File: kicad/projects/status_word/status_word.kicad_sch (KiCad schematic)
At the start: 54 parts, among them J1 peripheral_addr_bus_connector, J10 Conn_01x02_Pin, J11 Conn_01x02_Pin, J12 Conn_01x02_Pin, J13 Conn_01x02_Pin, J14 Conn_01x08_Socket, J15 Conn_01x03_Pin, J2 peripheral_aux_connector, J3 peripheral_membank_connector, J4 Conn_01x16_Socket, J5 Conn_01x04_Socket, J6 Conn_01x02_Pin, J7 Conn_01x02_Pin, J8 Conn_01x02_Pin, J9 Conn_01x02_Pin, U1 74HC10, U2 74HC377, U3 74HC377, U4 74HC245, U5 74HC245, U6 74HC245, U7 74HC245

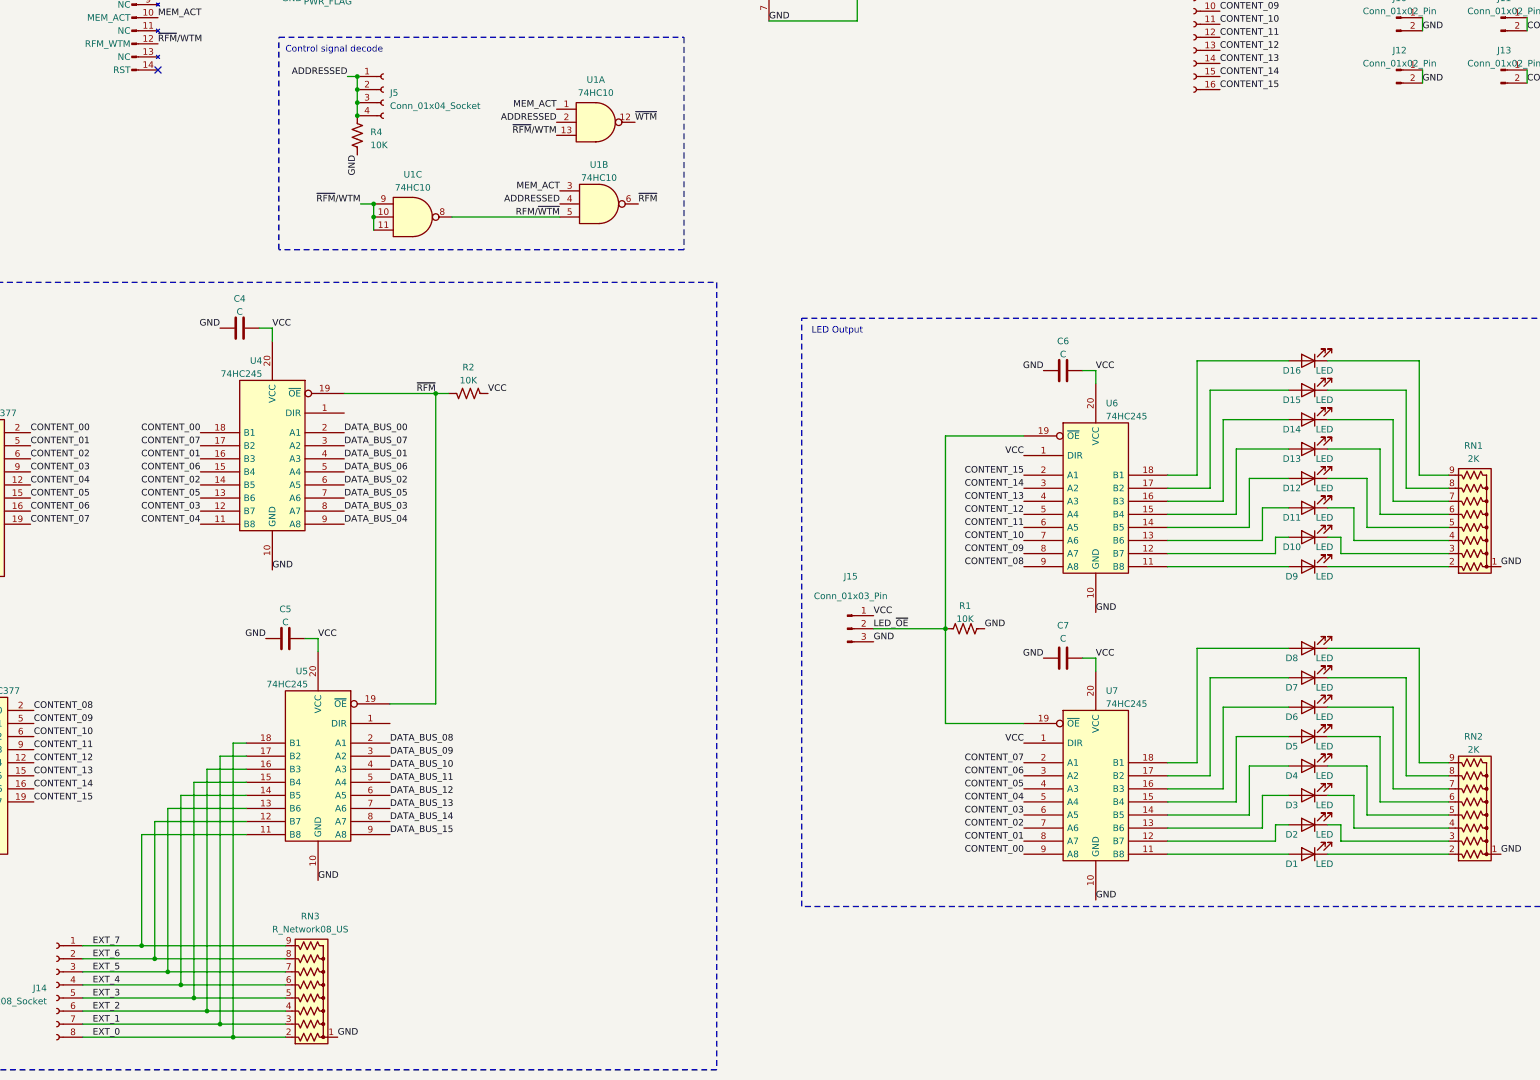
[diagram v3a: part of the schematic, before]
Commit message: Status word PCB done - just needs tech check.
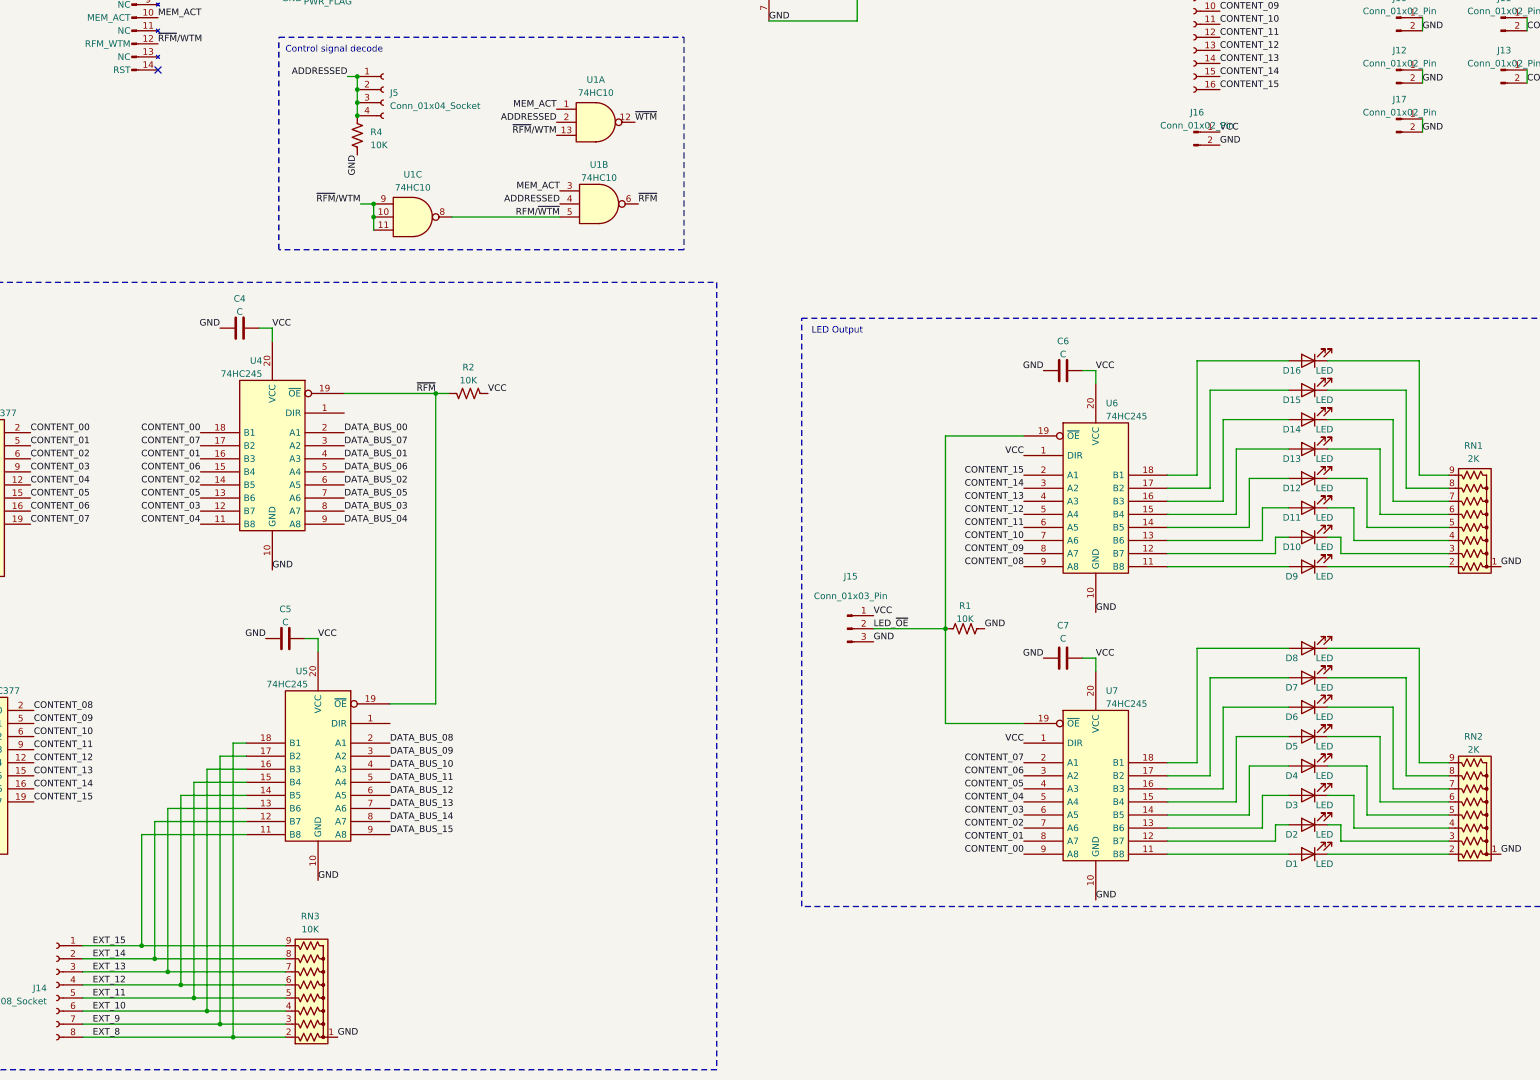
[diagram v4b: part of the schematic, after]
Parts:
- added J16: Conn_01x02_Pin, Connector_PinSocket_2.54mm:PinSocket_1x02_P2.54mm_Horizontal, symbol Connector:Conn_01x02_Pin
- added J17: Conn_01x02_Pin, Connector_PinHeader_2.54mm:PinHeader_1x02_P2.54mm_Vertical, symbol Connector:Conn_01x02_Pin
- RN3: value R_Network08_US -> 10K
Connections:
- net GND: now also J16.2 (Pin_2), J17.1 (Pin_1), J17.2 (Pin_2)
- net VCC: now also J16.1 (Pin_1)
- net EXT_0 renamed EXT_8
- net EXT_1 renamed EXT_9
- net EXT_2 renamed EXT_10
- net EXT_3 renamed EXT_11
- net EXT_4 renamed EXT_12
- net EXT_5 renamed EXT_13
- net EXT_6 renamed EXT_14
- net EXT_7 renamed EXT_15
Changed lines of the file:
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@@
+    (stroke (width 0) (type default))
+  )
+  (wire (pts (xy 360.045 67.945) (xy 360.045 70.485))
     (stroke (width 0) (type default))
   )
@@
     (effects (font (size 1.27 1.27)) (justify left bottom))
   )
-  (label "EXT_0" (at 101.6 246.38 0) (fields_autoplaced)
+  (label "EXT_8" (at 101.6 246.38 0) (fields_autoplaced)
     (effects (font (size 1.27 1.27)) (justify left bottom))
   )
@@
     (effects (font (size 1.27 1.27)) (justify left bottom))
   )
+  (label "VCC" (at 320.675 70.485 0) (fields_autoplaced)
+    (effects (font (size 1.27 1.27)) (justify left bottom))
+  )
   (label "CONTENT_09" (at 282.575 152.4 180) (fields_autoplaced)
     (effects (font (size 1.27 1.27)) (justify right bottom))
@@
     (effects (font (size 1.27 1.27)) (justify left bottom))
   )
-  (label "EXT_4" (at 101.6 236.22 0) (fields_autoplaced)
+  (label "EXT_12" (at 101.6 236.22 0) (fields_autoplaced)
     (effects (font (size 1.27 1.27)) (justify left bottom))
   )
@@
     (effects (font (size 1.27 1.27)) (justify left bottom))
   )
-  (label "EXT_7" (at 101.6 228.6 0) (fields_autoplaced)
+  (label "EXT_15" (at 101.6 228.6 0) (fields_autoplaced)
     (effects (font (size 1.27 1.27)) (justify left bottom))
   )
@@
     (effects (font (size 1.27 1.27)) (justify left bottom))
   )
-  (label "EXT_2" (at 101.6 241.3 0) (fields_autoplaced)
+  (label "EXT_10" (at 101.6 241.3 0) (fields_autoplaced)
     (effects (font (size 1.27 1.27)) (justify left bottom))
   )
@@
     (effects (font (size 1.27 1.27)) (justify right bottom))
   )
+  (label "GND" (at 360.045 70.485 0) (fields_autoplaced)
+    (effects (font (size 1.27 1.27)) (justify left bottom))
+  )
   (label "CONTENT_08" (at 320.675 44.45 0) (fields_autoplaced)
     (effects (font (size 1.27 1.27)) (justify left bottom))
   )
+  (label "GND" (at 320.675 73.025 0) (fields_autoplaced)
+    (effects (font (size 1.27 1.27)) (justify left bottom))
+  )
   (label "DATA_BUS_06" (at 64.135 144.145 180) (fields_autoplaced)
     (effects (font (size 1.27 1.27)) (justify right bottom))
@@
     (effects (font (size 1.27 1.27)) (justify right bottom))
   )
-  (label "EXT_1" (at 101.6 243.84 0) (fields_autoplaced)
+  (label "EXT_9" (at 101.6 243.84 0) (fields_autoplaced)
     (effects (font (size 1.27 1.27)) (justify left bottom))
   )
@@
     (effects (font (size 1.27 1.27)) (justify left bottom))
   )
-  (label "EXT_6" (at 101.6 231.14 0) (fields_autoplaced)
+  (label "EXT_14" (at 101.6 231.14 0) (fields_autoplaced)
     (effects (font (size 1.27 1.27)) (justify left bottom))
   )
@@
     (effects (font (size 1.27 1.27)) (justify right bottom))
   )
-  (label "EXT_5" (at 101.6 233.68 0) (fields_autoplaced)
+  (label "EXT_13" (at 101.6 233.68 0) (fields_autoplaced)
     (effects (font (size 1.27 1.27)) (justify left bottom))
   )
@@
     (effects (font (size 1.27 1.27)) (justify right bottom))
   )
-  (label "EXT_3" (at 101.6 238.76 0) (fields_autoplaced)
+  (label "EXT_11" (at 101.6 238.76 0) (fields_autoplaced)
     (effects (font (size 1.27 1.27)) (justify left bottom))
   )
@@
         (path "/0c25b387-1696-4e3f-ab8e-df646088b074"
           (reference "J15") (unit 1)
+        )
+      )
+    )
+  )
+  (symbol (lib_id "Connector:Conn_01x02_Pin") (at 354.965 67.945 0) (unit 1)
+    (in_bom yes) (on_board yes) (dnp no) (fields_autoplaced)
+    (property "Reference" "J17" (at 355.6 64.135 0)
+      (effects (font (size 1.27 1.27)))
+    )
+    (property "Value" "Conn_01x02_Pin" (at 355.6 66.675 0)
+      (effects (font (size 1.27 1.27)))
+    )
+    (property "Footprint" "Connector_PinHeader_2.54mm:PinHeader_1x02_P2.54mm_Vertical" (at 354.965 67.945 0)
+      (effects (font (size 1.27 1.27)) hide)
+    )
+    (property "Datasheet" "~" (at 354.965 67.945 0)
+      (effects (font (size 1.27 1.27)) hide)
+    )
+    (pin "1")
+    (pin "2")
+    (instances
+      (project "status_word"
+        (path "/0c25b387-1696-4e3f-ab8e-df646088b074"
+          (reference "J17") (unit 1)
         )
       )
@@
       (effects (font (size 1.27 1.27)))
     )
-    (property "Value" "R_Network08_US" (at 143.891 225.425 90)
+    (property "Value" "10K" (at 143.891 225.425 90)
       (effects (font (size 1.27 1.27)))
     )
@@
         )
       )
+    )
+  )
+  (symbol (lib_id "Connector:Conn_01x02_Pin") (at 315.595 70.485 0) (unit 1)
+    (in_bom yes) (on_board yes) (dnp no) (fields_autoplaced)
+    (property "Reference" "J16" (at 316.23 66.675 0)
+      (effects (font (size 1.27 1.27)))
+    )
+    (property "Value" "Conn_01x02_Pin" (at 316.23 69.215 0)
+      (effects (font (size 1.27 1.27)))
+    )
+    (property "Footprint" "Connector_PinSocket_2.54mm:PinSocket_1x02_P2.54mm_Horizontal" (at 315.595 70.485 0)
+      (effects (font (size 1.27 1.27)) hide)
+    )
+    (property "Datasheet" "~" (at 315.595 70.485 0)
+      (effects (font (size 1.27 1.27)) hide)
+    )
+    (pin "1")
+    (pin "2")
+    (instances
+      (project "status_word"
+        (path "/0c25b387-1696-4e3f-ab8e-df646088b074"
+          (reference "J16") (unit 1)
+        )
+      )

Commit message: Tech check on status word complete
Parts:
- C97, C98, C99: value C_Polarized -> 33uF
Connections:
- net GND: now also U4.1 (DIR), U5.1 (DIR)
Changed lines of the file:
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@@
 (kicad_sch (version 20230121) (generator eeschema)
   (paper "B")
+  (bus_alias "DATA_BUS" (members "DATA_BUS_00" "DATA_BUS_01" "DATA_BUS_02" "DATA_BUS_03" "DATA_BUS_04" "DATA_BUS_05" "DATA_BUS_06" "DATA_BUS_07" "DATA_BUS_08" "DATA_BUS_09" "DATA_BUS_10" "DATA_BUS_11" "DATA_BUS_12" "DATA_BUS_13" "DATA_BUS_14" "DATA_BUS_15"))
+  (bus_alias "BANK_BUS" (members "BANK_BUS_00" "BANK_BUS_01" "BANK_BUS_02" "BANK_BUS_03" "BANK_BUS_04" "BANK_BUS_05" "BANK_BUS_06" "BANK_BUS_07" "BANK_BUS_08" "BANK_BUS_09" "BANK_BUS_10" "BANK_BUS_11" "BANK_BUS_12" "BANK_BUS_13" "BANK_BUS_14" "BANK_BUS_15"))
   (bus_alias "ADDR_BUS" (members "ADDR_BUS_00" "ADDR_BUS_01" "ADDR_BUS_02" "ADDR_BUS_03" "ADDR_BUS_04" "ADDR_BUS_05" "ADDR_BUS_06" "ADDR_BUS_07" "ADDR_BUS_08" "ADDR_BUS_09" "ADDR_BUS_10" "ADDR_BUS_11" "ADDR_BUS_12" "ADDR_BUS_13" "ADDR_BUS_14" "ADDR_BUS_15"))
-  (bus_alias "BANK_BUS" (members "BANK_BUS_00" "BANK_BUS_01" "BANK_BUS_02" "BANK_BUS_03" "BANK_BUS_04" "BANK_BUS_05" "BANK_BUS_06" "BANK_BUS_07" "BANK_BUS_08" "BANK_BUS_09" "BANK_BUS_10" "BANK_BUS_11" "BANK_BUS_12" "BANK_BUS_13" "BANK_BUS_14" "BANK_BUS_15"))
-  (bus_alias "DATA_BUS" (members "DATA_BUS_00" "DATA_BUS_01" "DATA_BUS_02" "DATA_BUS_03" "DATA_BUS_04" "DATA_BUS_05" "DATA_BUS_06" "DATA_BUS_07" "DATA_BUS_08" "DATA_BUS_09" "DATA_BUS_10" "DATA_BUS_11" "DATA_BUS_12" "DATA_BUS_13" "DATA_BUS_14" "DATA_BUS_15"))
   (junction (at 126.365 243.84) (diameter 0) (color 0 0 0 0)
   )
@@
     (effects (font (size 1.27 1.27)) (justify right bottom))
   )
+  (label "GND" (at 159.385 185.42 0) (fields_autoplaced)
+    (effects (font (size 1.27 1.27)) (justify left bottom))
+  )
   (label "GND" (at 135.255 168.91 180) (fields_autoplaced)
     (effects (font (size 1.27 1.27)) (justify right bottom))
@@
   )
   (label "CONTENT_10" (at 320.675 49.53 0) (fields_autoplaced)
+    (effects (font (size 1.27 1.27)) (justify left bottom))
+  )
+  (label "GND" (at 150.495 125.095 0) (fields_autoplaced)
     (effects (font (size 1.27 1.27)) (justify left bottom))
   )
@@
       (effects (font (size 1.27 1.27)) (justify left))
     )
-    (property "Value" "C_Polarized" (at 165.1 37.211 0)
+    (property "Value" "33uF" (at 165.1 37.211 0)
       (effects (font (size 1.27 1.27)) (justify left))
     )
@@
       (effects (font (size 1.27 1.27)) (justify left))
     )
-    (property "Value" "C_Polarized" (at 203.835 37.211 0)
+    (property "Value" "33uF" (at 203.835 37.211 0)
       (effects (font (size 1.27 1.27)) (justify left))
     )
@@
       (effects (font (size 1.27 1.27)) (justify left))
     )
-    (property "Value" "C_Polarized" (at 184.785 37.211 0)
+    (property "Value" "33uF" (at 184.785 37.211 0)
       (effects (font (size 1.27 1.27)) (justify left))
     )
